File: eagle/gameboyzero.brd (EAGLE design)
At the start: 71 x 89 mm, 22 parts

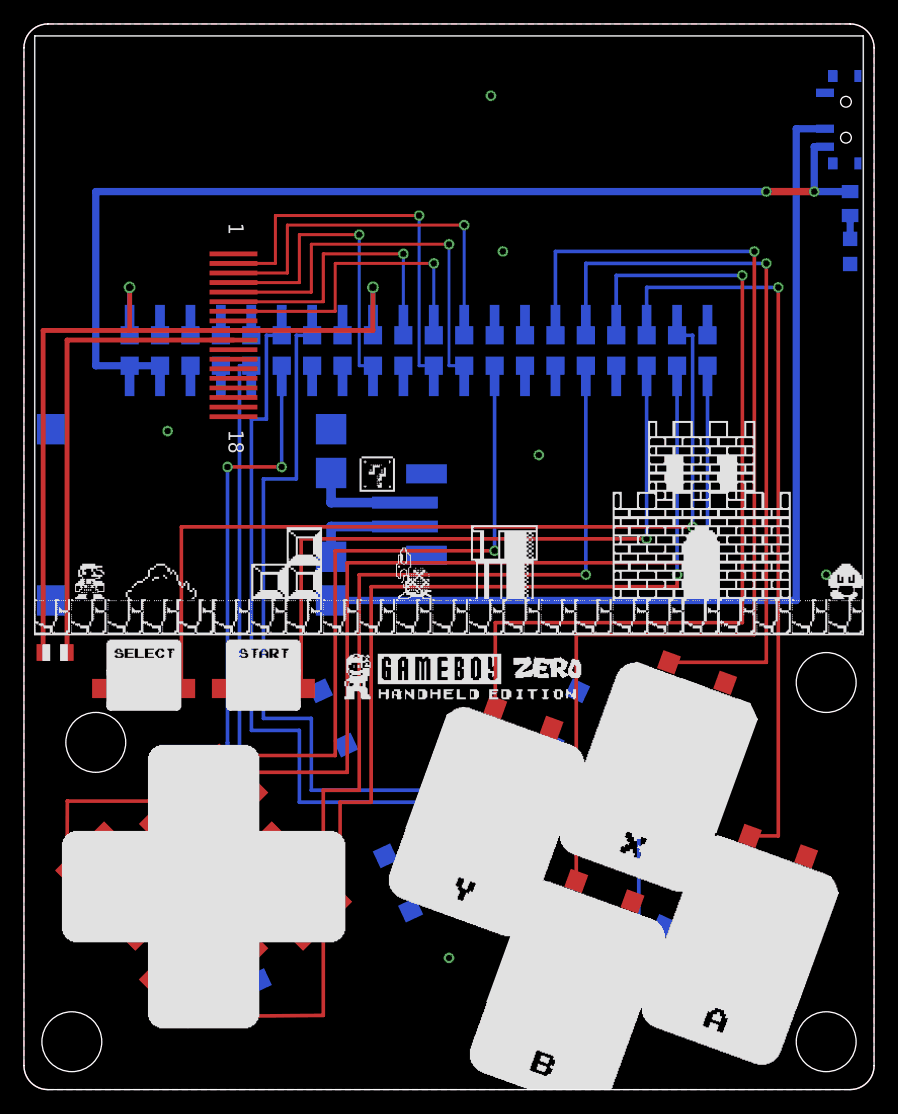
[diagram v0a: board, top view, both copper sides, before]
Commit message: Removed Copyrights and Trademarks
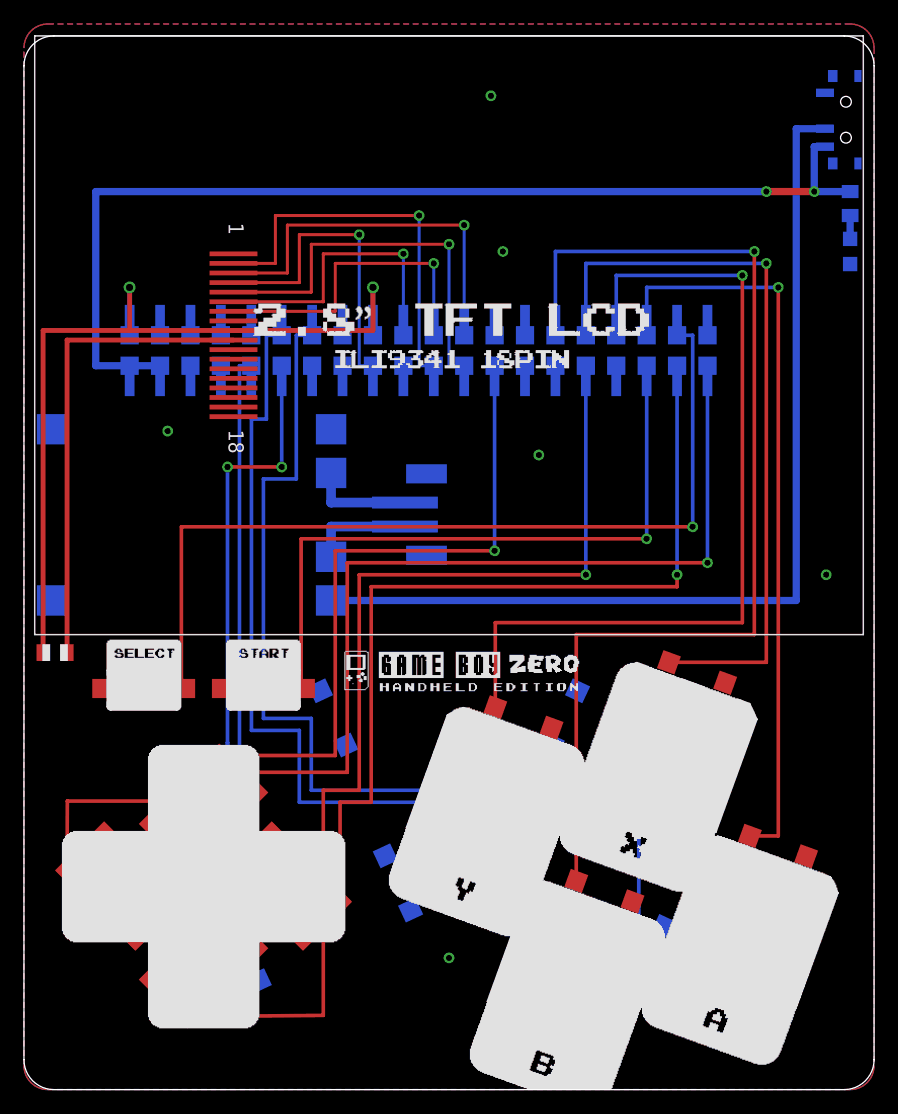
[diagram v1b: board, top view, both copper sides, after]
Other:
- board size 71 x 89 mm -> 71 x 88 mm

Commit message: updates
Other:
- board size 71 x 88 mm -> 71 x 89 mm
